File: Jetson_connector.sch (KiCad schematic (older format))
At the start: 1 part, among them J2 QTH-060-01-L-D-A

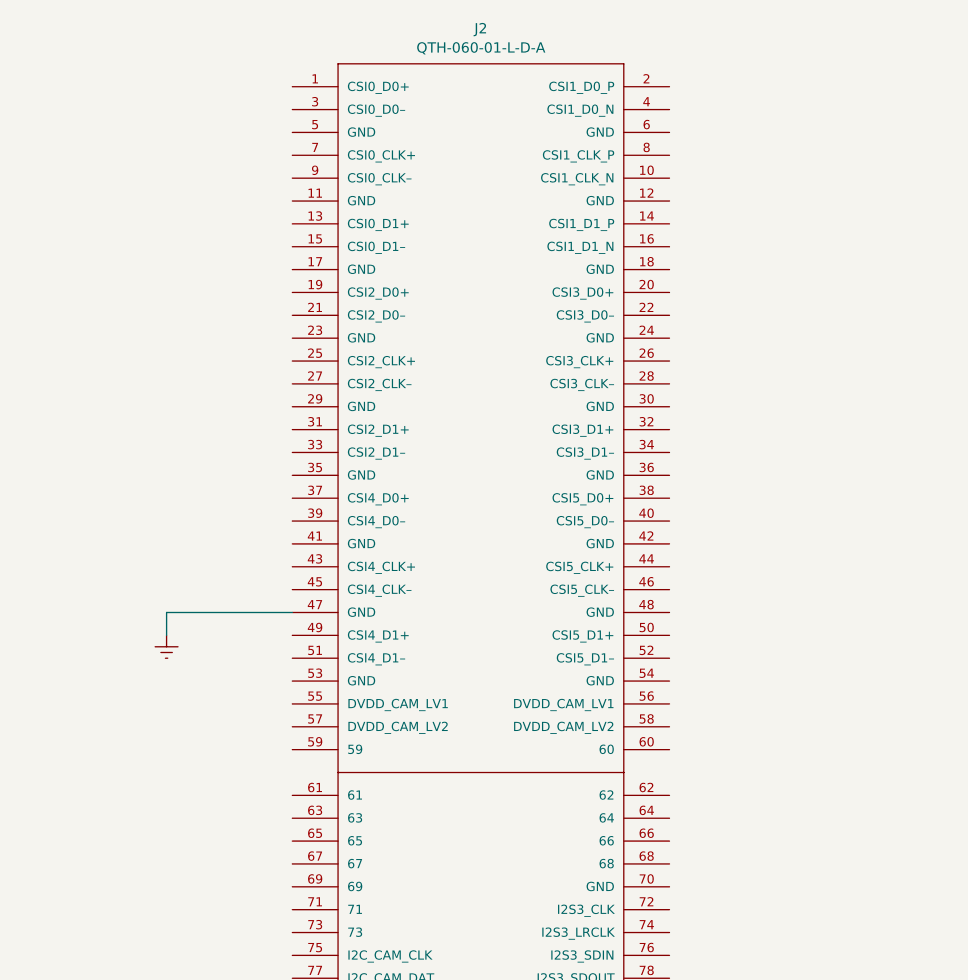
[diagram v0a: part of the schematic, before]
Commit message: Good, before replacing the swithches to TI ones
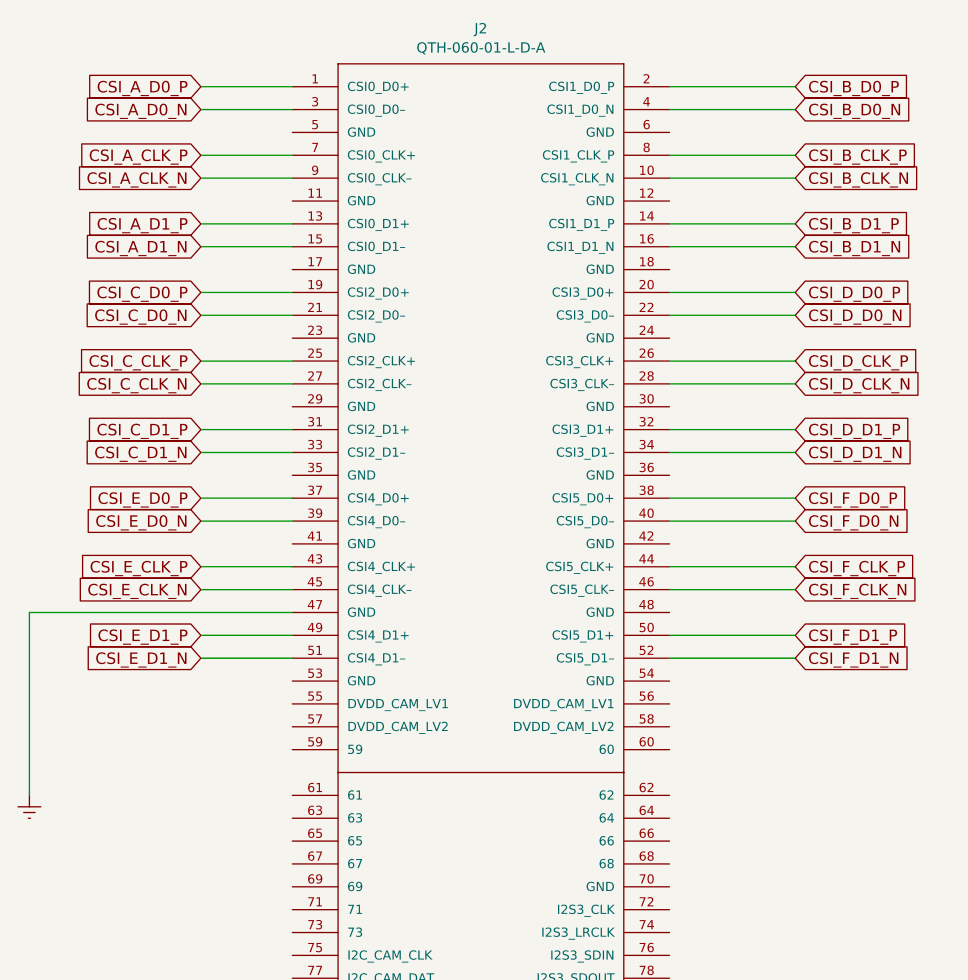
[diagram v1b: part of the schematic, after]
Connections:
- net CSI_A_D0_P: now reaches J2.1 (CSI0_D0+)
- net CSI_B_CLK_N: now reaches J2.10 (CSI1_CLK_N)
- net CSI_A_D1_P: now reaches J2.13 (CSI0_D1+)
- net CSI_B_D1_P: now reaches J2.14 (CSI1_D1_P)
- net CSI_A_D1_N: now reaches J2.15 (CSI0_D1–)
- net CSI_B_D1_N: now reaches J2.16 (CSI1_D1_N)
- net CSI_C_D0_P: now reaches J2.19 (CSI2_D0+)
- net CSI_B_D0_P: now reaches J2.2 (CSI1_D0_P)
- net CSI_D_D0_P: now reaches J2.20 (CSI3_D0+)
- net CSI_C_D0_N: now reaches J2.21 (CSI2_D0–)
- net CSI_D_D0_N: now reaches J2.22 (CSI3_D0–)
- net CSI_C_CLK_P: now reaches J2.25 (CSI2_CLK+)
- net CSI_D_CLK_P: now reaches J2.26 (CSI3_CLK+)
- net CSI_C_CLK_N: now reaches J2.27 (CSI2_CLK–)
- net CSI_D_CLK_N: now reaches J2.28 (CSI3_CLK–)
- net CSI_A_D0_N: now reaches J2.3 (CSI0_D0–)
- net CSI_C_D1_P: now reaches J2.31 (CSI2_D1+)
- net CSI_D_D1_P: now reaches J2.32 (CSI3_D1+)
- net CSI_C_D1_N: now reaches J2.33 (CSI2_D1–)
- net CSI_D_D1_N: now reaches J2.34 (CSI3_D1–)
- net CSI_E_D0_P: now reaches J2.37 (CSI4_D0+)
- net CSI_F_D0_P: now reaches J2.38 (CSI5_D0+)
- net CSI_E_D0_N: now reaches J2.39 (CSI4_D0–)
- net CSI_B_D0_N: now reaches J2.4 (CSI1_D0_N)
- net CSI_F_D0_N: now reaches J2.40 (CSI5_D0–)
- net CSI_E_CLK_P: now reaches J2.43 (CSI4_CLK+)
- net CSI_F_CLK_P: now reaches J2.44 (CSI5_CLK+)
- net CSI_E_CLK_N: now reaches J2.45 (CSI4_CLK–)
- net CSI_F_CLK_N: now reaches J2.46 (CSI5_CLK–)
- net CSI_E_D1_P: now reaches J2.49 (CSI4_D1+)
- net CSI_F_D1_P: now reaches J2.50 (CSI5_D1+)
- net CSI_E_D1_N: now reaches J2.51 (CSI4_D1–)
- net CSI_F_D1_N: now reaches J2.52 (CSI5_D1–)
- net CSI_A_CLK_P: now reaches J2.7 (CSI0_CLK+)
- net CSI_B_CLK_P: now reaches J2.8 (CSI1_CLK_P)
- net CSI_A_CLK_N: now reaches J2.9 (CSI0_CLK–)
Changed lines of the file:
@@
 $Descr A4 11693 8268
 encoding utf-8
-Sheet 3 46
+Sheet 3 32
 Title ""
 Date ""
@@
 $EndComp
 $Comp
-L power:Earth #PWR0103
+L power:Earth #PWR03
 U 1 1 61B10B3D
-P 4100 3300
-F 0 "#PWR0103" H 4100 3050 50  0001 C CNN
-F 1 "Earth" H 4100 3150 50  0001 C CNN
-F 2 "" H 4100 3300 50  0001 C CNN
-F 3 "~" H 4100 3300 50  0001 C CNN
-	1    4100 3300
+P 3500 4000
+F 0 "#PWR03" H 3500 3750 50  0001 C CNN
+F 1 "Earth" H 3500 3850 50  0001 C CNN
+F 2 "" H 3500 4000 50  0001 C CNN
+F 3 "~" H 3500 4000 50  0001 C CNN
+	1    3500 4000
 	1    0    0    -1
 $EndComp
 Wire Wire Line
-	4650 3200 4100 3200
+	4650 3200 3500 3200
 Wire Wire Line
-	4100 3200 4100 3300
+	3500 3200 3500 4000
+Wire Wire Line
+	4650 900  4250 900
+Wire Wire Line
+	4650 1000 4250 1000
+Wire Wire Line
+	4650 1200 4250 1200
+Wire Wire Line
+	4650 1300 4250 1300
+Wire Wire Line
+	4650 1500 4250 1500
+Wire Wire Line
+	4650 1600 4250 1600
+Wire Wire Line
+	6300 900  6850 900
+Wire Wire Line
+	6300 1000 6850 1000
+Wire Wire Line
+	6300 1200 6850 1200
+Wire Wire Line
+	6300 1300 6850 1300
+Wire Wire Line
+	6300 1500 6850 1500
+Wire Wire Line
+	6300 1600 6850 1600
+Text GLabel 4250 900  0    50   Input ~ 0
+CSI_A_D0_P
+Text GLabel 4250 1000 0    50   Input ~ 0
+CSI_A_D0_N
+Text GLabel 4250 1200 0    50   Input ~ 0
+CSI_A_CLK_P
+Text GLabel 4250 1300 0    50   Input ~ 0
+CSI_A_CLK_N
+Text GLabel 4250 1500 0    50   Input ~ 0
+CSI_A_D1_P
+Text GLabel 4250 1600 0    50   Input ~ 0
+CSI_A_D1_N
+Text GLabel 6850 1000 2    50   Input ~ 0
+CSI_B_D0_N
+Text GLabel 6850 1200 2    50   Input ~ 0
+CSI_B_CLK_P
+Text GLabel 6850 1300 2    50   Input ~ 0
+CSI_B_CLK_N
+Text GLabel 6850 1500 2    50   Input ~ 0
+CSI_B_D1_P
+Text GLabel 6850 1600 2    50   Input ~ 0
+CSI_B_D1_N
+Wire Wire Line
+	4650 1800 4250 1800
+Wire Wire Line
+	4650 1900 4250 1900
+Wire Wire Line
+	4650 2100 4250 2100
+Wire Wire Line
+	4650 2200 4250 2200
+Wire Wire Line
+	4650 2400 4250 2400
+Wire Wire Line
+	4650 2500 4250 2500
+Wire Wire Line
+	6300 1800 6850 1800
+Wire Wire Line
+	6300 1900 6850 1900
+Wire Wire Line
+	6300 2100 6850 2100
+Wire Wire Line
+	6300 2200 6850 2200
+Wire Wire Line
+	6300 2400 6850 2400
+Wire Wire Line
+	6300 2500 6850 2500
+Text GLabel 4250 1800 0    50   Input ~ 0
+CSI_C_D0_P
+Text GLabel 4250 1900 0    50   Input ~ 0
+CSI_C_D0_N
+Text GLabel 4250 2100 0    50   Input ~ 0
+CSI_C_CLK_P
+Text GLabel 4250 2200 0    50   Input ~ 0
+CSI_C_CLK_N
+Text GLabel 4250 2400 0    50   Input ~ 0
+CSI_C_D1_P
+Text GLabel 4250 2500 0    50   Input ~ 0
+CSI_C_D1_N
+Text GLabel 6850 1800 2    50   Input ~ 0
+CSI_D_D0_P
+Text GLabel 6850 1900 2    50   Input ~ 0
+CSI_D_D0_N
+Text GLabel 6850 2100 2    50   Input ~ 0
+CSI_D_CLK_P
+Text GLabel 6850 2200 2    50   Input ~ 0
+CSI_D_CLK_N
+Text GLabel 6850 2400 2    50   Input ~ 0
+CSI_D_D1_P
+Text GLabel 6850 2500 2    50   Input ~ 0
+CSI_D_D1_N
+Text GLabel 6850 900  2    50   Input ~ 0
+CSI_B_D0_P
+Wire Wire Line
+	4650 2700 4250 2700
+Wire Wire Line
+	4650 2800 4250 2800
+Wire Wire Line
+	4650 3000 4250 3000
+Wire Wire Line
+	4650 3100 4250 3100
+Wire Wire Line
+	4650 3300 4250 3300
+Wire Wire Line
+	4650 3400 4250 3400
+Wire Wire Line
+	6300 2700 6850 2700
+Wire Wire Line
+	6300 2800 6850 2800
+Wire Wire Line
+	6300 3000 6850 3000
+Wire Wire Line
+	6300 3100 6850 3100
+Wire Wire Line
+	6300 3300 6850 3300
+Wire Wire Line
+	6300 3400 6850 3400
+Text GLabel 4250 2700 0    50   Input ~ 0
+CSI_E_D0_P
+Text GLabel 4250 2800 0    50   Input ~ 0
+CSI_E_D0_N
+Text GLabel 4250 3000 0    50   Input ~ 0
+CSI_E_CLK_P
+Text GLabel 4250 3100 0    50   Input ~ 0
+CSI_E_CLK_N
+Text GLabel 4250 3300 0    50   Input ~ 0
+CSI_E_D1_P
+Text GLabel 4250 3400 0    50   Input ~ 0
+CSI_E_D1_N
+Text GLabel 6850 2700 2    50   Input ~ 0
+CSI_F_D0_P
+Text GLabel 6850 2800 2    50   Input ~ 0
+CSI_F_D0_N
+Text GLabel 6850 3000 2    50   Input ~ 0
+CSI_F_CLK_P
+Text GLabel 6850 3100 2    50   Input ~ 0
+CSI_F_CLK_N
+Text GLabel 6850 3300 2    50   Input ~ 0
+CSI_F_D1_P
+Text GLabel 6850 3400 2    50   Input ~ 0
+CSI_F_D1_N
 $EndSCHEMATC

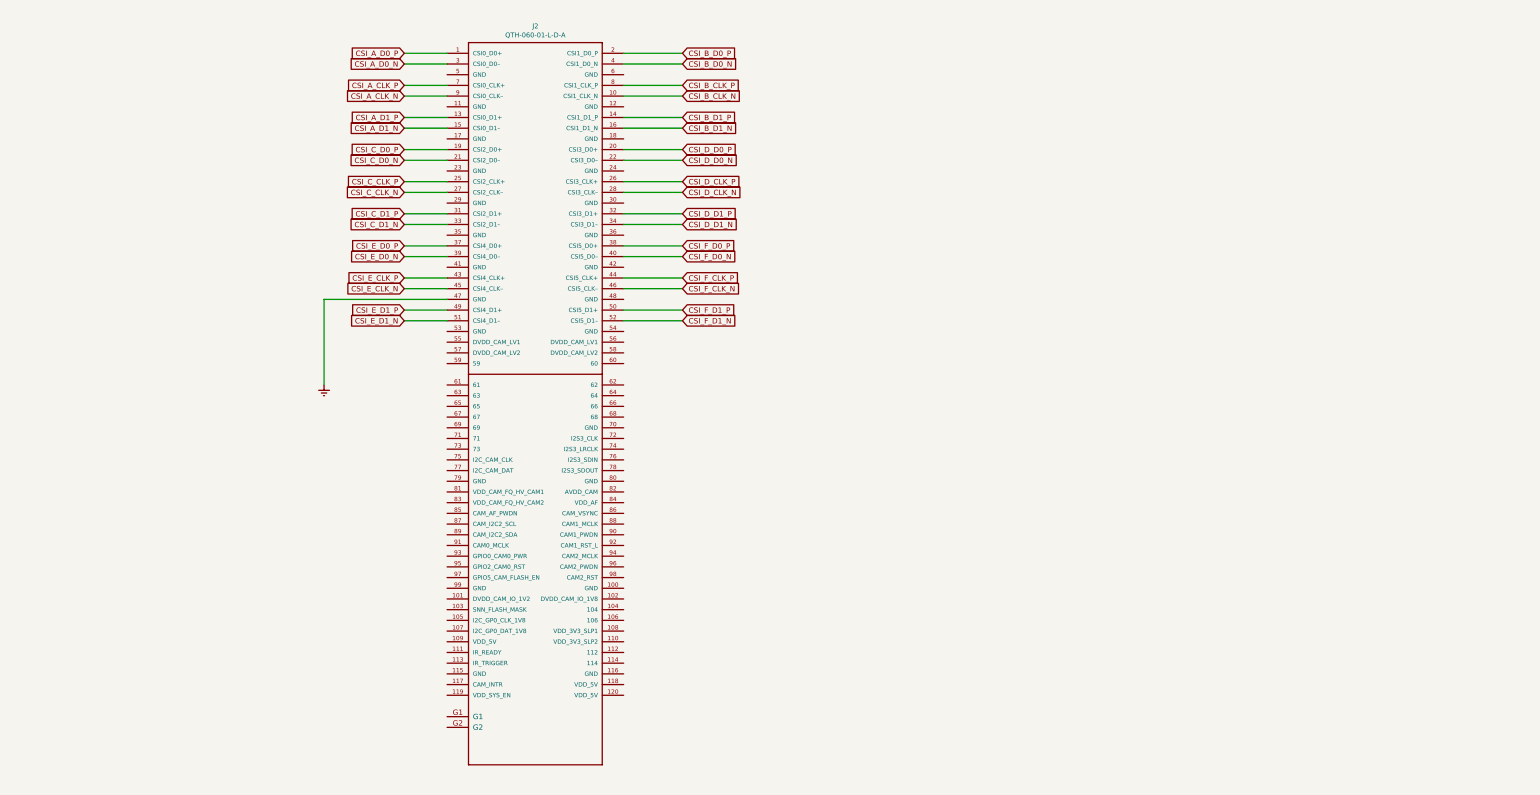
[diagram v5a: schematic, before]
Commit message: added EEPROM
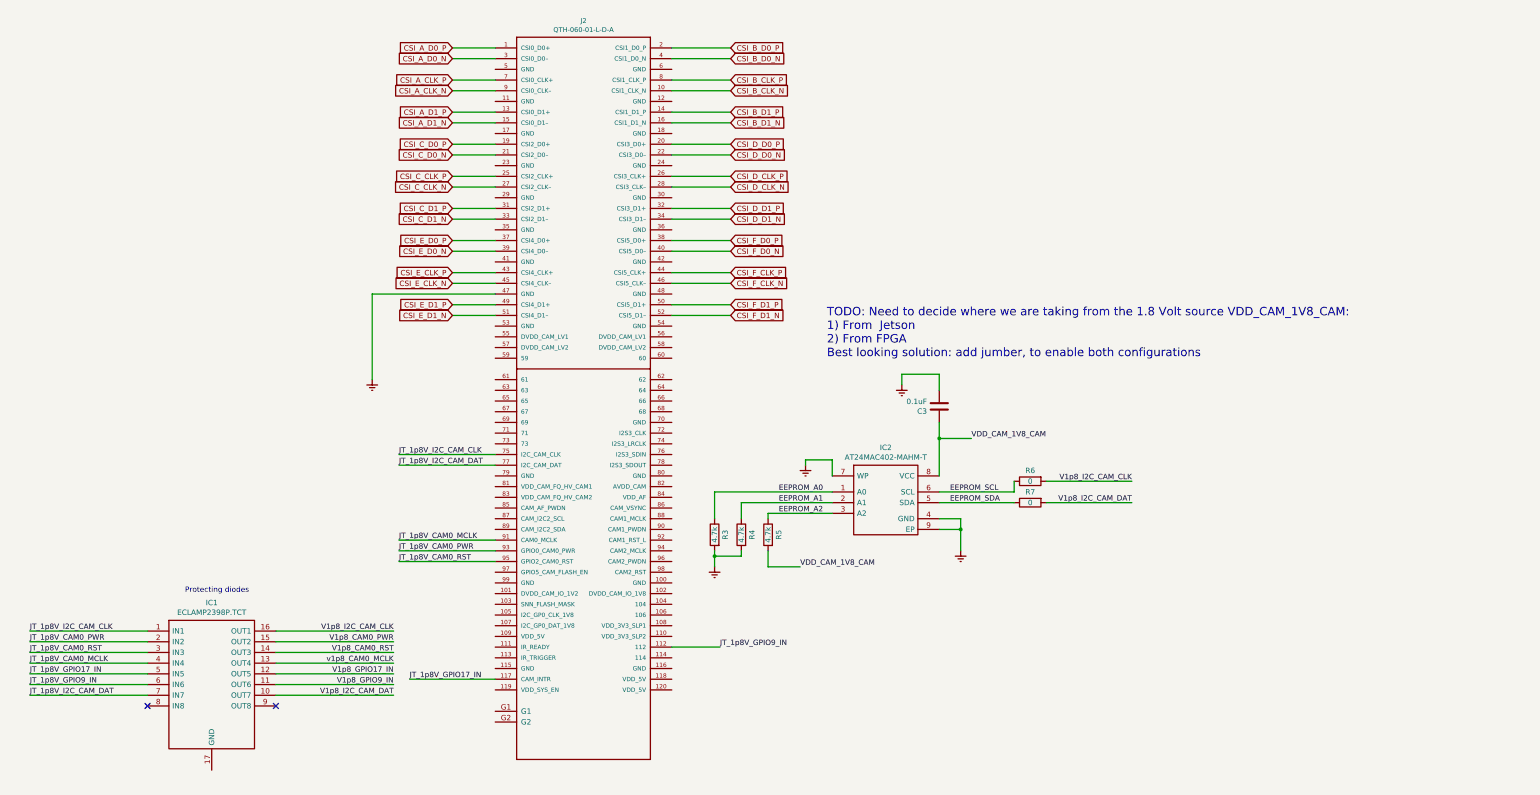
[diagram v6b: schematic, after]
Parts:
- added C3: 0.1uF, Capacitors_SMD:C_0402, symbol FMC_MIPI_v2:C
- added IC1: ECLAMP2398P.TCT, SON50P160X400X65-17N, symbol FMC_MIPI_v2:ECLAMP2398P.TCT
- added IC2: AT24MAC402-MAHM-T, SON50P300X200X60-9N, symbol FMC_MIPI_v2:AT24MAC402-MAHM-T
- added R3, R4, R5: 4.7k, Resistors_SMD:R_0805, symbol Device:R
- added R6, R7: 0, Resistors_SMD:R_0805, symbol Device:R
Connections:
- net Earth: now also C3.2, IC2.4 (GND), IC2.7 (WP), IC2.9 (EP), R3.2, R4.2
- net JT_1p8V_GPIO9_IN: now reaches J2.112
- net JT_1p8V_GPIO9_IN: now also IC1.6 (IN6)
- net JT_1p8V_GPIO17_IN: now reaches J2.117 (CAM_INTR)
- net JT_1p8V_GPIO17_IN: now also IC1.5 (IN5)
- net JT_1p8V_I2C_CAM_CLK: now reaches J2.75 (I2C_CAM_CLK)
- net JT_1p8V_I2C_CAM_CLK: now also IC1.1 (IN1)
- net JT_1p8V_I2C_CAM_DAT: now reaches J2.77 (I2C_CAM_DAT)
- net JT_1p8V_I2C_CAM_DAT: now also IC1.7 (IN7)
- net JT_1p8V_CAM0_MCLK: now reaches J2.91 (CAM0_MCLK)
- net JT_1p8V_CAM0_MCLK: now also IC1.4 (IN4)
- net JT_1p8V_CAM0_PWR: now reaches J2.93 (GPIO0_CAM0_PWR)
- net JT_1p8V_CAM0_PWR: now also IC1.2 (IN2)
- net JT_1p8V_CAM0_RST: now reaches J2.95 (GPIO2_CAM0_RST)
- net JT_1p8V_CAM0_RST: now also IC1.3 (IN3)
- new net EEPROM_A0: IC2.1 (A0), R3.1
- new net EEPROM_A1: IC2.2 (A1), R4.1
- new net EEPROM_A2: IC2.3 (A2), R5.1
- new net EEPROM_SCL: IC2.6 (SCL), R6.1
- new net EEPROM_SDA: IC2.5 (SDA), R7.1
- new net V1p8_CAM0_PWR: IC1.15 (OUT2)
- new net V1p8_CAM0_RST: IC1.14 (OUT3)
- new net V1p8_GPIO17_IN: IC1.12 (OUT5)
- new net V1p8_GPIO9_IN: IC1.11 (OUT6)
- new net V1p8_I2C_CAM_CLK: IC1.16 (OUT1), R6.2
- new net V1p8_I2C_CAM_DAT: IC1.10 (OUT7), R7.2
- new net VDD_CAM_1V8_CAM: C3.1, IC2.8 (VCC), R5.2
- new net v1p8_CAM0_MCLK: IC1.13 (OUT4)
- no-connect marks 0 -> 2
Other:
- note added: "Protecting diodes"
- note added: "TODO: Need to decide where we are taking from the 1.8 Volt source VDD_CAM_1V8_CAM:\n1) From Jetson\n2) From FPGA\nBest looking solution: add jumber, to enable both configurations"
- moved on the sheet: J2

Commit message: added more level shifters and power 1.8 Volt
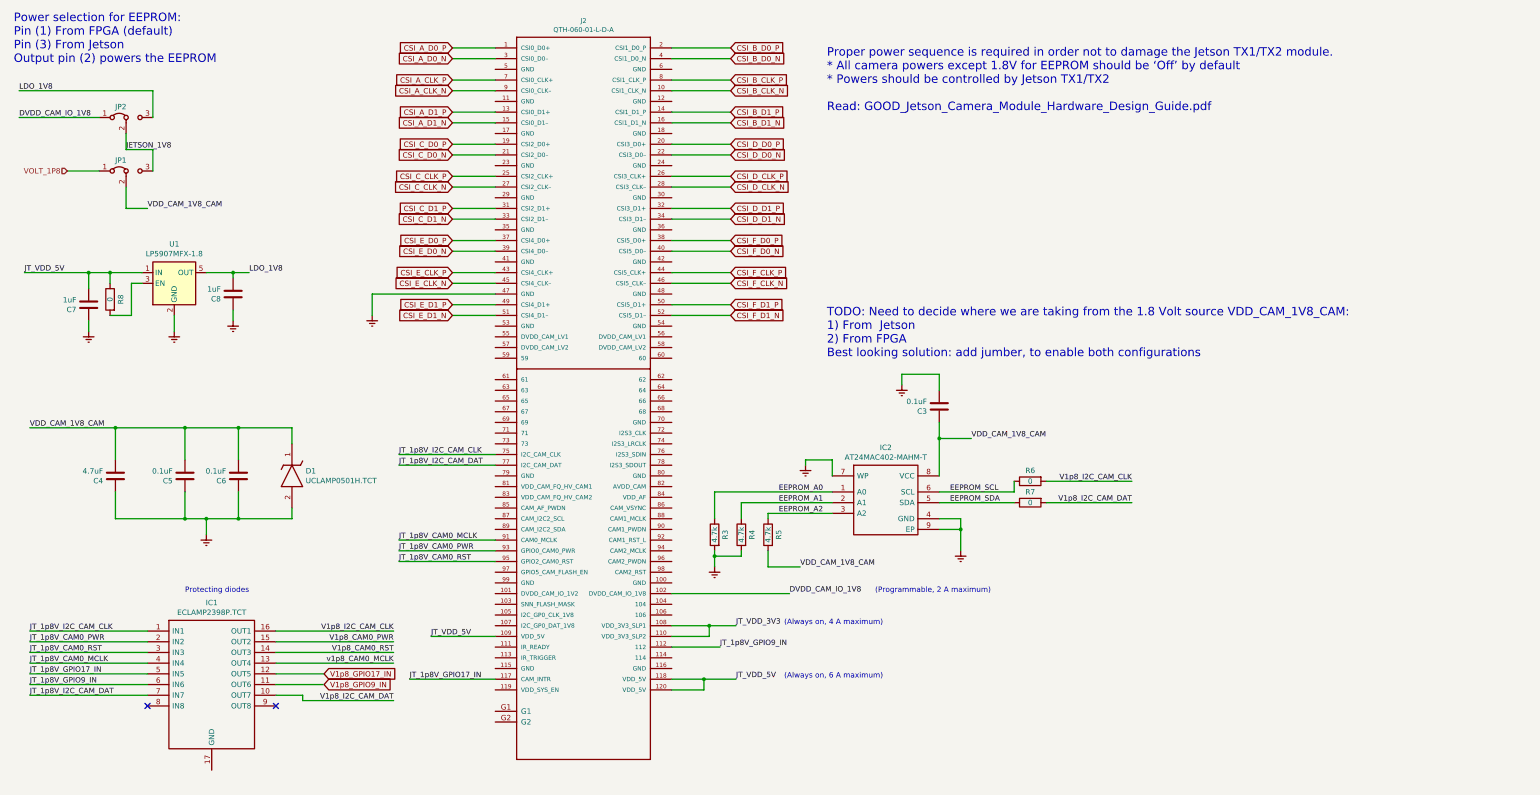
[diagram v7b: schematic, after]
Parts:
- added C4: 4.7uF, Capacitors_SMD:C_0805, symbol FMC_MIPI_v2:C
- added C5, C6: 0.1uF, Capacitors_SMD:C_0402, symbol FMC_MIPI_v2:C
- added C7, C8: 1uF, Capacitors_SMD:C_0805, symbol FMC_MIPI_v2:C
- added D1: UCLAMP0501H.TCT, Diodes_SMD:D_SOD-523, symbol FMC_MIPI_v2:UCLAMP0501H.TCT
- added JP1, JP2: Jumper_3_Bridged12, Pin_Headers:Pin_Header_Straight_1x03_Pitch2.54mm, symbol Jumper:Jumper_3_Bridged12
- added R8: 0, Resistors_SMD:R_0805, symbol Device:R
- added U1: LP5907MFX-1.8, TO_SOT_Packages_SMD:SOT-23-5, symbol Regulator_Linear:LP5907MFX-1.8
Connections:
- net Earth: now also C4.1, C5.1, C6.1, C7.1, C8.1, D1.2, U1.2 (GND)
- net VDD_CAM_1V8_CAM: now also C4.2, C5.2, C6.2, D1.1, JP1.2 (C)
- net DVDD_CAM_IO_1V8: now reaches J2.102 (DVDD_CAM_IO_1V8)
- net DVDD_CAM_IO_1V8: now also JP2.1 (A)
- net JT_VDD_3V3: now reaches J2.108 (VDD_3V3_SLP1)
- net JT_VDD_3V3: now also J2.110 (VDD_3V3_SLP2)
- net JT_VDD_5V: now reaches J2.109 (VDD_5V)
- net JT_VDD_5V: now also J2.118 (VDD_5V), J2.120 (VDD_5V), C7.2, R8.1, U1.1 (IN)
- new net: R8.2, U1.3 (EN)
- new net JETSON_1V8: JP1.3 (B), JP2.2 (C)
- new net LDO_1V8: C8.2, JP2.3 (B), U1.5 (OUT)
- new net VOLT_1P8: JP1.1 (A)
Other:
- note added: "(Always on, 4 A maximum)"
- note added: "(Always on, 6 A maximum)"
- note added: "(Programmable, 2 A maximum)"
- note added: "Power selection for EEPROM:\nPin (1) From FPGA (default)\nPin (3) From Jetson\nOutput pin (2) powers the EEPROM\n"
- note added: "Proper power sequence is required in order not to damage the Jetson TX1/TX2 module.\n* All camera powers except 1.8V for EEPROM should be ‘Off’ by default\n* Powers should be controlled by Jetson TX1/TX2\n\nRead: GOOD_Jetson_Camera_Module_Hardware_Design_Guide.pdf"

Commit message: minor changes 4
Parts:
- removed IC1: ECLAMP2398P.TCT, SON50P160X400X65-17N, symbol FMC_MIPI_v2:ECLAMP2398P.TCT
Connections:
- no-connect marks 2 -> 0
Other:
- note added: "Power LDO 1.8 Volt, 250 mA"
- note removed: "Protecting diodes"
- moved on the sheet: C7, C8, JP1, JP2, R8, U1
